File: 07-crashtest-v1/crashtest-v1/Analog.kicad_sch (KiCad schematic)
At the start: 12 parts, among them U1 INA827AIDGK, U10 INA827AIDGK, U11 INA827AIDGK, U12 INA827AIDGK, U2 INA827AIDGK, U3 INA827AIDGK, U4 INA827AIDGK, U5 INA827AIDGK, U6 INA827AIDGK, U7 INA827AIDGK, U8 INA827AIDGK, U9 INA827AIDGK

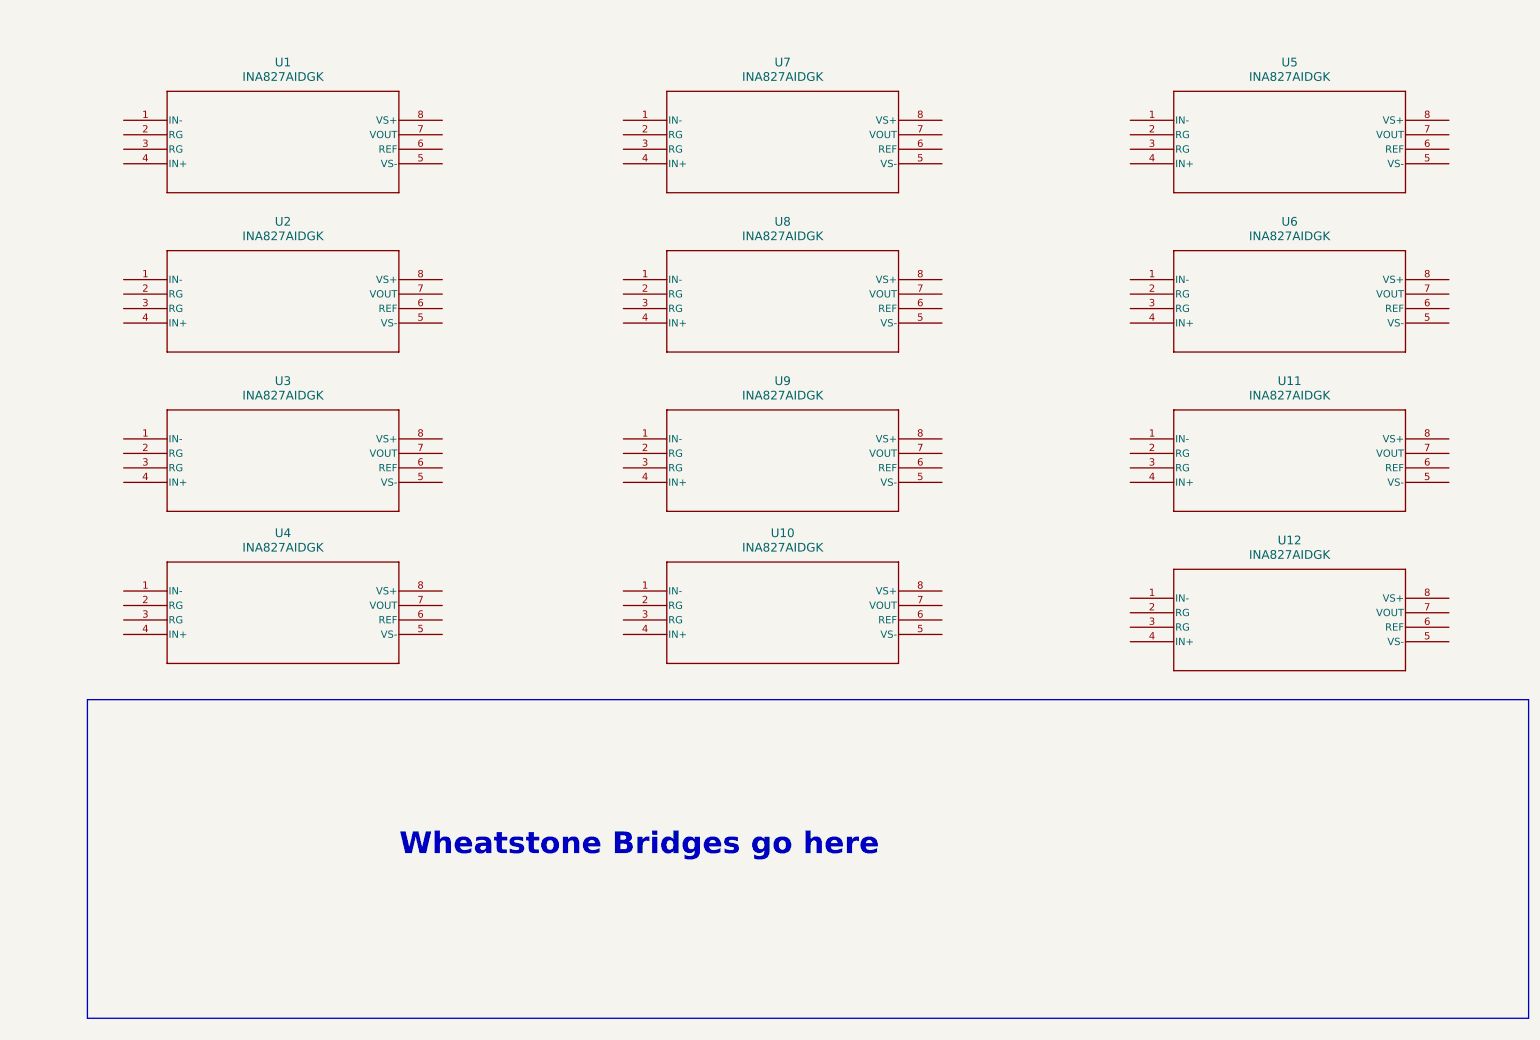
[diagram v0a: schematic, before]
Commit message: added 12 higharchical sheets for each of the rossetts
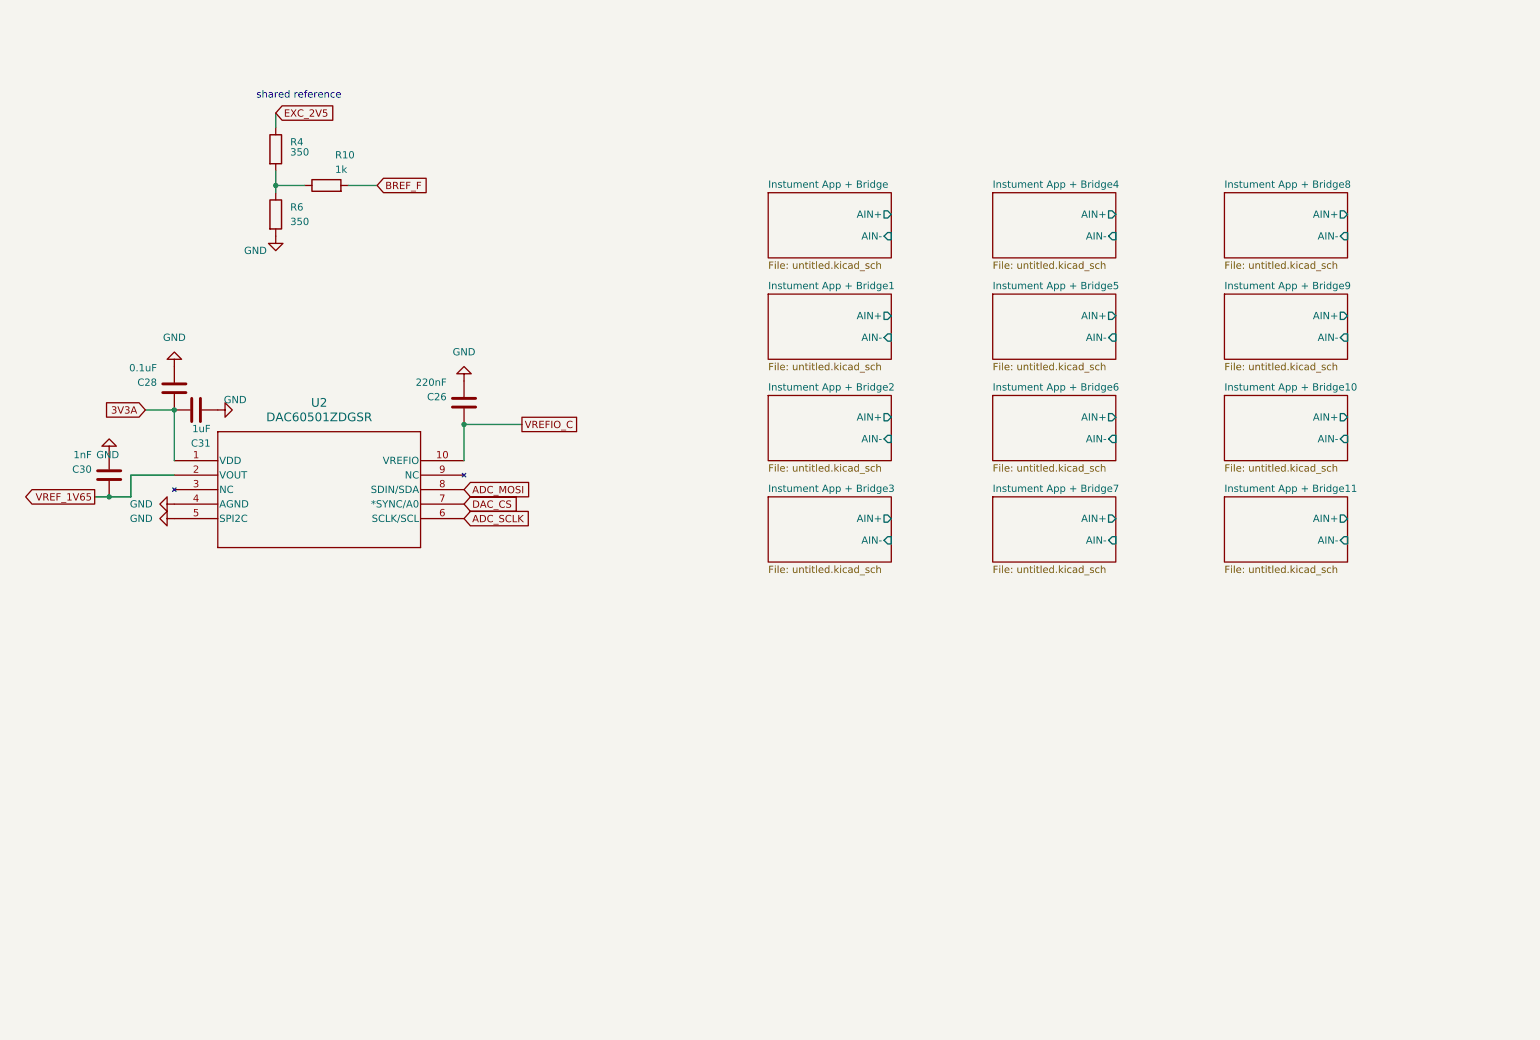
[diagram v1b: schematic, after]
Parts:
- removed U1, U10, U11, U12, U2, U3, U4, U5, U6, U7, U8, U9: INA827AIDGK, DGK8_TEX, symbol 1-Crashtest:INA827AIDGK
- added C26: 220nF, Capacitor_SMD:C_0402_1005Metric_Pad0.74x0.62mm_HandSolder, symbol Device:C
- added C28: 0.1uF, Capacitor_SMD:C_0402_1005Metric_Pad0.74x0.62mm_HandSolder, symbol Device:C
- added C30: 1nF, Capacitor_SMD:C_0402_1005Metric_Pad0.74x0.62mm_HandSolder, symbol Device:C
- added C31: 1uF, Capacitor_SMD:C_0402_1005Metric_Pad0.74x0.62mm_HandSolder, symbol Device:C
- added R10: 1k, Resistor_SMD:R_0402_1005Metric_Pad0.72x0.64mm_HandSolder, symbol Device:R
- added R4, R6: 350, Resistor_SMD:R_0402_1005Metric_Pad0.72x0.64mm_HandSolder, symbol Device:R
- added U2: DAC60501ZDGSR, Package_SO:MSOP-10_3x3mm_P0.5mm, symbol my-symbols:DAC60501MDGSR
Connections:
- new net: R10.1, R4.2, R6.1
- new net 3V3A: C28.2, C31.2, U2.1 (VDD)
- new net ADC_MOSI: U2.8 (SDIN/SDA)
- new net ADC_SCLK: U2.6 (SCLK/SCL)
- new net BREF_F: R10.2
- new net DAC_CS: U2.7 (*SYNC/A0)
- new net EXC_2V5: R4.1
- new net GND: C26.1, C28.1, C30.1, C31.1, R6.2, U2.4 (AGND), U2.5 (SPI2C)
- new net VREFIO_C: C26.2, U2.10 (VREFIO)
- new net VREF_1V65: C30.2, U2.2 (VOUT)
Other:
- added sheet Instument App + Bridge (untitled.kicad_sch)
- added sheet Instument App + Bridge1 (untitled.kicad_sch)
- added sheet Instument App + Bridge10 (untitled.kicad_sch)
- added sheet Instument App + Bridge11 (untitled.kicad_sch)
- added sheet Instument App + Bridge2 (untitled.kicad_sch)
- added sheet Instument App + Bridge3 (untitled.kicad_sch)
- added sheet Instument App + Bridge4 (untitled.kicad_sch)
- added sheet Instument App + Bridge5 (untitled.kicad_sch)
- added sheet Instument App + Bridge6 (untitled.kicad_sch)
- added sheet Instument App + Bridge7 (untitled.kicad_sch)
- added sheet Instument App + Bridge8 (untitled.kicad_sch)
- added sheet Instument App + Bridge9 (untitled.kicad_sch)
- note added: "shared reference"
- note removed: "Wheatstone Bridges go here"

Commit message: stuff
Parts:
- added C51, C56: 1uF, Capacitor_SMD:C_0603_1608Metric, symbol Device:C
- added C52, C53, C54, C55, C57: 0.1uF, Capacitor_SMD:C_0603_1608Metric, symbol Device:C
- added IC2: AD7175-8BCPZ-RL7, footprints:AD7175-8BCPZ-RL7, symbol symbols:AD7175-8BCPZ-RL7
- added R65: 10k, Resistor_SMD:R_0603_1608Metric, symbol Device:R
- added TP7: MISO_adc, TestPoint:TestPoint_Pad_1.0x1.0mm, symbol Connector:TestPoint
- added TP8: MOSI_adc, TestPoint:TestPoint_Pad_1.0x1.0mm, symbol Connector:TestPoint
- added TP9: SCLK_adc, TestPoint:TestPoint_Pad_1.0x1.0mm, symbol Connector:TestPoint
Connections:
- new net: C56.1, C57.2, IC2.22 (REGCAPD)
- new net: C51.2, C52.2, IC2.7 (REGCAPA)
- new net !CS_adc: IC2.17 (~{CS}), R65.1
- new net !ERROR_adc: IC2.18 (~{ERROR})
- new net 3.3V_teensy: C55.1, IC2.20 (IOVDD), R65.2
- new net 5V_stable: C53.1, C54.1, IC2.10 (AVDD2), IC2.40 (REF+), IC2.9 (AVDD1)
- new net AIN0: IC2.2 (AIN0/REF2-)
- new net GNDA: C51.1, C52.1, C53.2, IC2.11 (PDSW), IC2.8 (AVSS)
- new net GNDD: C54.2, C55.2, C56.2, C57.1, IC2.19 (~{SYNC}), IC2.21 (DGND), IC2.39 (REF-), IC2.41 (EP)
- new net MISO_adc: IC2.14 (DOUT/~{RDY}), TP7.1
- new net MOSI_adc: IC2.15 (DIN), TP8.1
- new net SCLK_adc: IC2.16 (SCLK), TP9.1
- no-connect marks 0 -> 4
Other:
- sheet Instument App + Bridge ports: added AIN; removed AIN+, AIN-
- sheet Instument App + Bridge1 ports: added AIN; removed AIN+, AIN-
- sheet Instument App + Bridge10 ports: added AIN; removed AIN+, AIN-
- sheet Instument App + Bridge11 ports: added AIN; removed AIN+, AIN-
- sheet Instument App + Bridge2 ports: added AIN; removed AIN+, AIN-
- sheet Instument App + Bridge3 ports: added AIN; removed AIN+, AIN-
- sheet Instument App + Bridge4 ports: added AIN; removed AIN+, AIN-
- sheet Instument App + Bridge5 ports: added AIN; removed AIN+, AIN-
- sheet Instument App + Bridge6 ports: added AIN; removed AIN+, AIN-
- sheet Instument App + Bridge7 ports: added AIN; removed AIN+, AIN-
- sheet Instument App + Bridge8 ports: added AIN; removed AIN+, AIN-
- sheet Instument App + Bridge9 ports: added AIN; removed AIN+, AIN-
- note added: "ADC"
- moved on the sheet: C26, C28, C30, C31, R10, R4, R6, U2

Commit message: stuff
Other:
- moved on the sheet: C30
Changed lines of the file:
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@@
+	)
+	(junction
+		(at 27.94 43.18)
+		(diameter 0)
+		(color 0 0 0 0)
 	)
 	(junction
@@
 	)
 	(junction
-		(at 27.94 43.18)
-		(diameter 0)
-		(color 0 0 0 0)
-	)
-	(junction
 		(at 66.04 133.35)
 		(diameter 0)
@@
 	(wire
 		(pts
-			(xy 31.75 43.18) (xy 27.94 43.18)
-		)
-		(stroke
-			(width 0)
-			(type default)
-		)
-	)
-	(wire
-		(pts
 			(xy 130.81 118.11) (xy 134.62 118.11)
 		)
@@
 		(pts
 			(xy 228.6 46.99) (xy 233.68 46.99)
+		)
+		(stroke
+			(width 0)
+			(type default)
+		)
+	)
+	(wire
+		(pts
+			(xy 27.94 43.18) (xy 31.75 43.18)
 		)
 		(stroke
@@
 	(symbol
 		(lib_id "power:GND")
-		(at 27.94 35.56 180)
+		(at 27.94 50.8 0)
 		(unit 1)
 		(body_style 1)
@@
 		(dnp no)
 		(property "Reference" "#PWR063"
-			(at 27.94 29.21 0)
+			(at 27.94 57.15 0)
 			(hide yes)
 			(show_name no)
@@
 		)
 		(property "Value" "GND"
-			(at 27.686 35.814 0)
+			(at 28.194 50.546 0)
 			(show_name no)
 			(do_not_autoplace no)
@@
 		)
 		(property "Footprint" ""
-			(at 27.94 35.56 0)
+			(at 27.94 50.8 0)
 			(hide yes)
 			(show_name no)
@@
 		)
 		(property "Datasheet" ""
-			(at 27.94 35.56 0)
+			(at 27.94 50.8 0)
 			(hide yes)
 			(show_name no)
@@
 		)
 		(property "Description" "Power symbol creates a global label with name \"GND\" , ground"
-			(at 27.94 35.56 0)
+			(at 27.94 50.8 0)
 			(hide yes)
 			(show_name no)
@@
 	(symbol
 		(lib_id "Device:C")
-		(at 27.94 39.37 0)
+		(at 27.94 46.99 180)
 		(unit 1)
 		(body_style 1)
@@
 		(dnp no)
 		(property "Reference" "C30"
-			(at 24.892 38.354 0)
+			(at 21.336 45.72 0)
 			(show_name no)
 			(do_not_autoplace no)
@@
 		)
 		(property "Value" "1nF"
-			(at 24.892 35.814 0)
+			(at 21.336 48.26 0)
 			(show_name no)
 			(do_not_autoplace no)
@@
 		)
 		(property "Footprint" "Capacitor_SMD:C_0402_1005Metric_Pad0.74x0.62mm_HandSolder"
-			(at 28.9052 43.18 0)
+			(at 26.9748 43.18 0)
 			(hide yes)
 			(show_name no)
@@
 		)
 		(property "Datasheet" ""
-			(at 27.94 39.37 0)
+			(at 27.94 46.99 0)
 			(hide yes)
 			(show_name no)
@@
 		)
 		(property "Description" "Unpolarized capacitor"
-			(at 27.94 39.37 0)
-			(hide yes)
-			(show_name no)
+			(at 27.94 46.99 0)
+			(hide yes)
+			(show_name no)
